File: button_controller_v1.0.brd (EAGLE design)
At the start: 160 x 100 mm, 88 parts, among them IC2 4051D, IC3 4520D, IC5 4051D

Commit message: Finished tracing
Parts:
- moved R6 18.4 mm to (74.3, 11.1)
- moved R1 14.3 mm to (78.7, 18.1), turned to 0 degrees
- moved R2 14.3 mm to (74.3, 18.1)
- moved R3 14.3 mm to (69.8, 18.1), turned to 0 degrees
- moved D14 11.1 mm to (11.4, 29.8)
- moved D17 11.1 mm to (37.5, 37.8)
- moved D22 11.1 mm to (37.5, 29.8)
- moved D25 11.1 mm to (24.4, 37.8)
- moved D30 11.1 mm to (24.4, 29.8)
- moved D33 11.1 mm to (63.5, 37.8)
- moved D38 11.1 mm to (63.5, 29.8)
- moved D41 11.1 mm to (50.5, 37.8)
- moved D46 11.1 mm to (50.5, 29.8)
- moved D57 11.1 mm to (76.5, 37.8)
- moved D62 11.1 mm to (76.5, 29.8)
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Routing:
- net +5V: track 75.1 -> 243.3 mm, vias 3 -> 7
- net RESET: track 0.00 -> 119.3 mm, vias 0 -> 4
- net CLK: track 0.00 -> 105.5 mm
- net BUTTON_VAL_CHAIN_2: track 0.00 -> 101.8 mm
- net BUTTON_VAL_CHAIN_4: track 0.00 -> 100.8 mm
- net BUTTON_VAL_CHAIN_1: track 0.00 -> 96.2 mm
- net BUTTON_VAL_CHAIN_3: track 0.00 -> 95.2 mm
- net BUTTON_VAL_CHAIN_5: track 0.00 -> 94.1 mm
- net BUTTON_VALUE: track 32.7 -> 105.8 mm, vias 2 -> 4
- net ROW7: track 33.5 -> 70.1 mm
- net ROW6: track 36.2 -> 67.6 mm, vias 0 -> 2
- net COL3: track 202.0 -> 178.3 mm
- net ROW5: track 32.1 -> 49.9 mm, vias 0 -> 2
- net COL2: track 189.1 -> 176.0 mm
- net COL4: track 212.9 -> 200.3 mm, vias 10 -> 8
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- added copper zone on layer 16, net GND
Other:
- board size 160 x 100 mm -> 105.7 x 44.1 mm

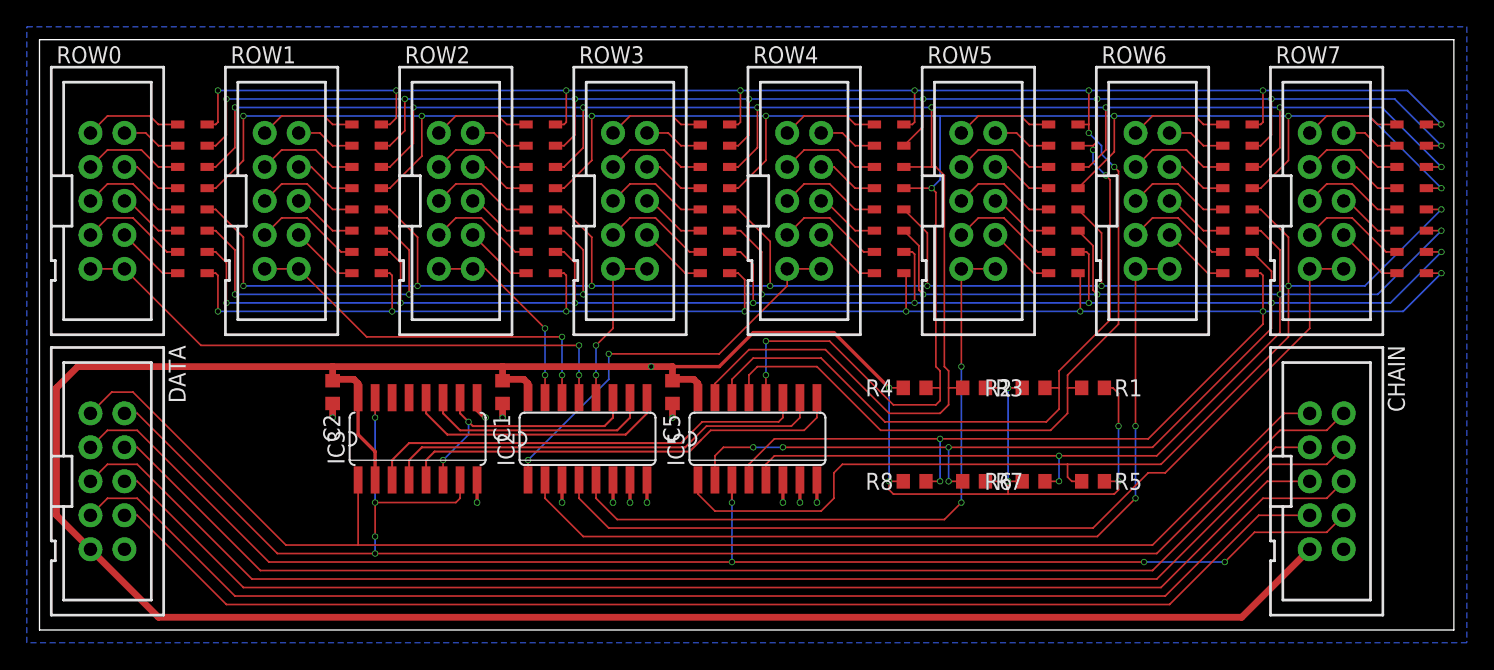
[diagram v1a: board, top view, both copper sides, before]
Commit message: Massive rerouting for a clearer separation between x and y direction
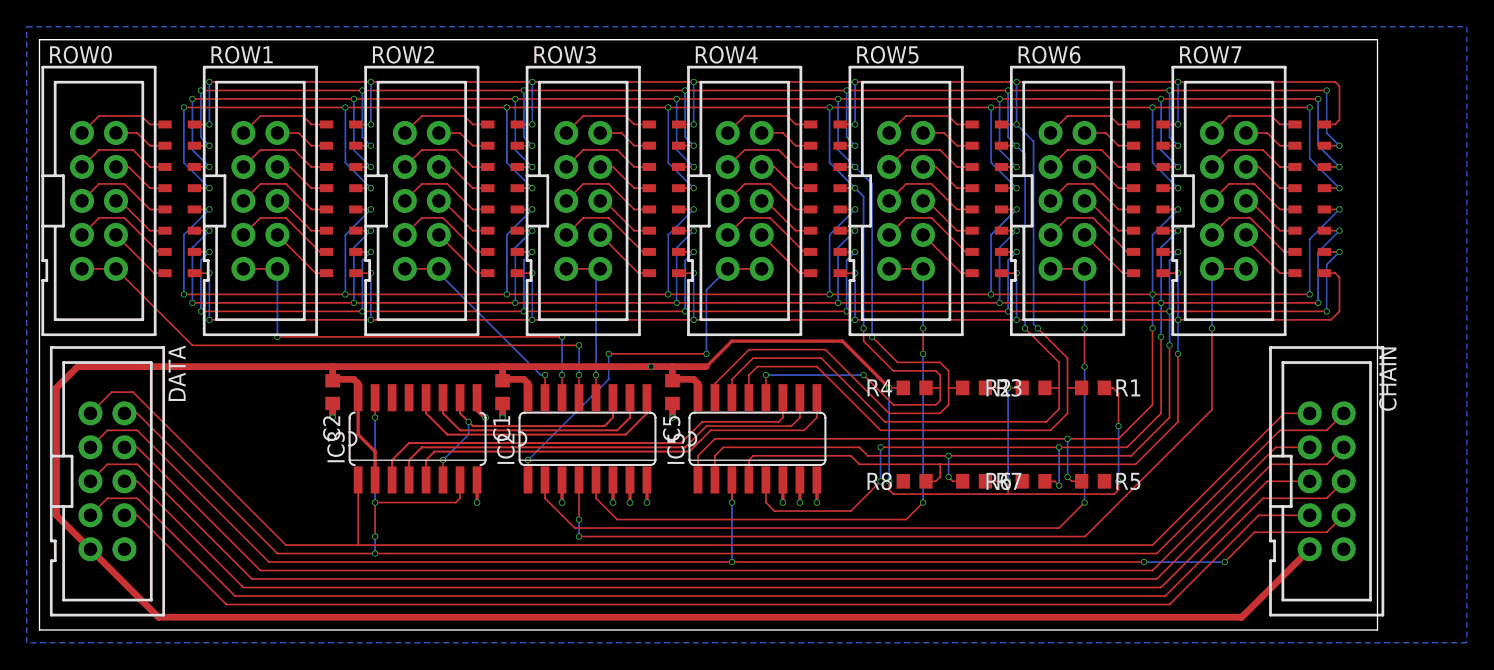
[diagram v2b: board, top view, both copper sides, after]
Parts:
- moved D89 7.62 mm to (94.9, 37.8)
- moved D90 7.62 mm to (94.9, 36.2)
- moved D91 7.62 mm to (94.9, 34.6)
- moved D92 7.62 mm to (94.9, 33.0)
- moved D93 7.62 mm to (94.9, 31.4)
- moved D94 7.62 mm to (94.9, 29.8)
- moved D95 7.62 mm to (94.9, 28.3)
- moved D96 7.62 mm to (94.9, 26.7)
- moved ROW7 7.30 mm to (88.9, 32.1)
- moved D73 6.67 mm to (82.9, 37.8)
- moved D74 6.67 mm to (82.9, 36.2)
- moved D75 6.67 mm to (82.9, 34.6)
- moved D76 6.67 mm to (82.9, 33.0)
- moved D77 6.67 mm to (82.9, 31.4)
- moved D78 6.67 mm to (82.9, 29.8)
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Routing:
- net COL2: track 176.0 -> 184.0 mm, vias 8 -> 17
- net COL3: track 178.3 -> 185.2 mm, vias 10 -> 19
- net COL5: track 183.7 -> 189.1 mm, vias 10 -> 21
- net ROW1: track 28.9 -> 33.8 mm, vias 2 -> 3
- net ROW6: track 67.6 -> 63.4 mm, vias 2 -> 3
- net +5V: track 243.3 -> 239.6 mm
- net COL1: track 176.3 -> 179.3 mm, vias 10 -> 17
- net ROW5: track 49.9 -> 47.0 mm, vias 2 -> 3
- net COL0: track 170.0 -> 172.4 mm, vias 10 -> 15
- net ROW4: track 31.2 -> 28.8 mm, vias 2 -> 3
- net ROW7: track 70.1 -> 68.5 mm, vias 0 -> 3
- net COL6: track 179.1 -> 179.8 mm, vias 12 -> 19
- net ROW2: track 15.0 -> 15.6 mm, vias 2 -> 1
- net ROW0: track 42.8 -> 43.4 mm
- net COL7: track 166.7 -> 167.3 mm, vias 10 -> 15
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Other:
- board size 105.7 x 44.1 mm -> 100 x 44.1 mm

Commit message: As small as it gets
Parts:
- moved R5 5.02 mm to (74.0, 9.53), turned to 270 degrees
- moved R1 4.77 mm to (74.0, 17.8), turned to 90 degrees
- moved R6 3.27 mm to (71.4, 9.53), turned to 270 degrees
- moved R2 2.88 mm to (71.4, 17.8), turned to 90 degrees
- moved R8 2.03 mm to (66.7, 9.53), turned to 270 degrees
- moved R7 1.71 mm to (69.2, 9.53), turned to 270 degrees
- moved D12 1.59 mm to (10.5, 31.4)
- moved D13 1.59 mm to (10.5, 29.8)
- moved D16 1.59 mm to (10.5, 25.1)
- moved D20 1.59 mm to (34.6, 31.4)
- moved D21 1.59 mm to (34.6, 29.8)
- moved D24 1.59 mm to (34.6, 25.1)
- moved D28 1.59 mm to (22.5, 31.4)
- moved D29 1.59 mm to (22.5, 29.8)
- moved D32 1.59 mm to (22.5, 25.1)
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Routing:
- net +5V: track 239.6 -> 231.9 mm, vias 7 -> 6
- net COL5: track 189.1 -> 182.3 mm
- net COL3: track 185.2 -> 178.8 mm
- net COL1: track 179.3 -> 173.9 mm
- net COL6: track 179.8 -> 175.6 mm
- net COL7: track 167.3 -> 163.2 mm
- net COL4: track 200.0 -> 196.3 mm
- net CLK: track 105.5 -> 109.1 mm
- net ROW7: track 68.5 -> 64.9 mm
- net BUTTON_VAL_CHAIN_1: track 96.2 -> 99.8 mm
- net BUTTON_VAL_CHAIN_2: track 101.8 -> 105.2 mm
- net BUTTON_VAL_CHAIN_3: track 95.2 -> 98.4 mm
- net RESET: track 119.3 -> 122.4 mm
- net COL0: track 172.4 -> 169.4 mm
- net BUTTON_VAL_CHAIN_4: track 100.8 -> 103.8 mm
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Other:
- board size 100 x 44.1 mm -> 100 x 40.6 mm

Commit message: Finished everything
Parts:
- added U$1: (no value), joakim:XONIK_LOGO_60
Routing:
- net ROW5: track 45.7 -> 43.4 mm, vias 1 -> 3
- net ROW6: track 62.1 -> 60.3 mm
- net COL3: track 178.8 -> 177.3 mm, vias 19 -> 18
- net +5V: track 231.9 -> 233.1 mm
- net COL_A: track 34.2 -> 33.3 mm
- net COL0: track 169.4 -> 170.3 mm
- net ROW2: track 15.9 -> 15.2 mm
- net COL1: track 173.9 -> 174.4 mm
- net COL7: track 163.2 -> 163.5 mm, vias 15 -> 14
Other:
- board text added: "+V"
- board text added: "4VOB"
- board text added: "8 x 8 key matrix scanner v1.0"
- board text added: "C1"
- board text added: "C2"
- board text added: "C3"
- board text added: "C4"
- board text added: "C5"
- board text added: "CLK"
- board text added: "GND"
- board text added: "Pin 1-8 = COL0-7 Pin 9,10 = ROW"
- board text added: "RST"
- board text added: "VAL"

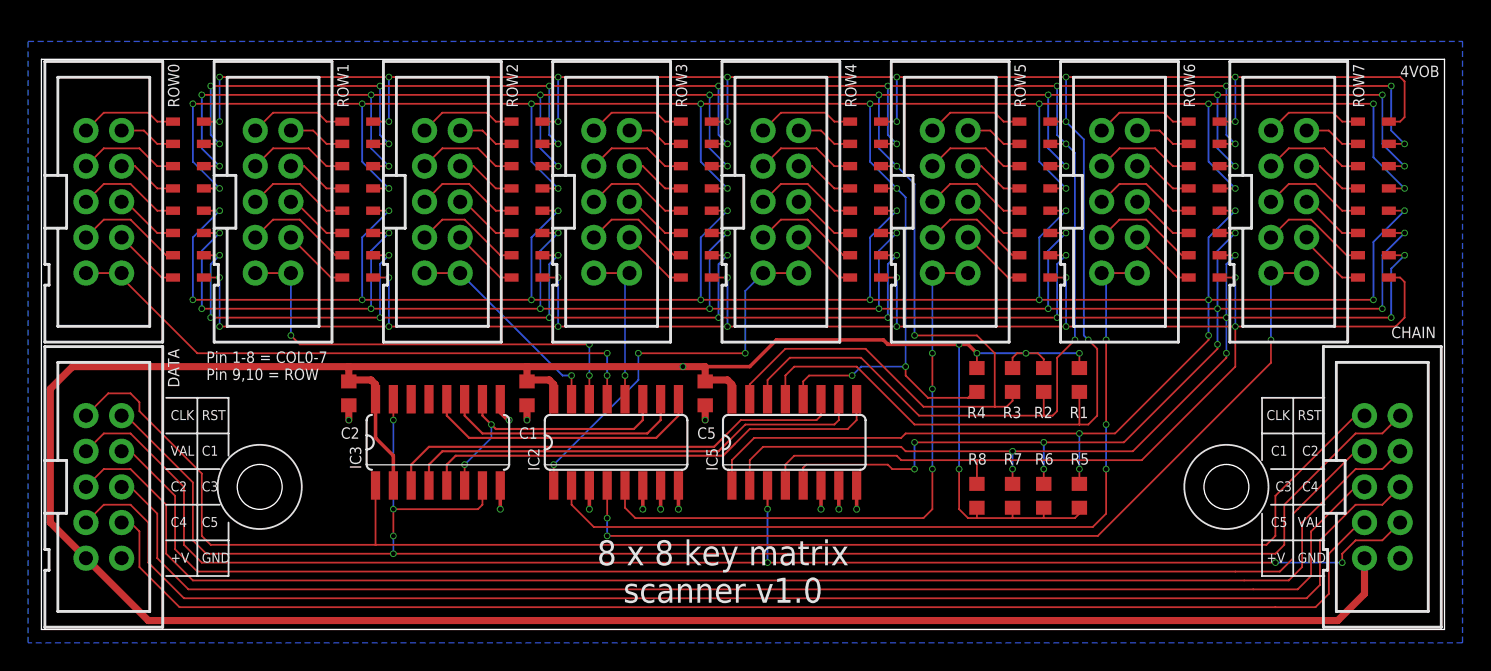
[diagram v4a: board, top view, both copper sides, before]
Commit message: Updated IDC connector size
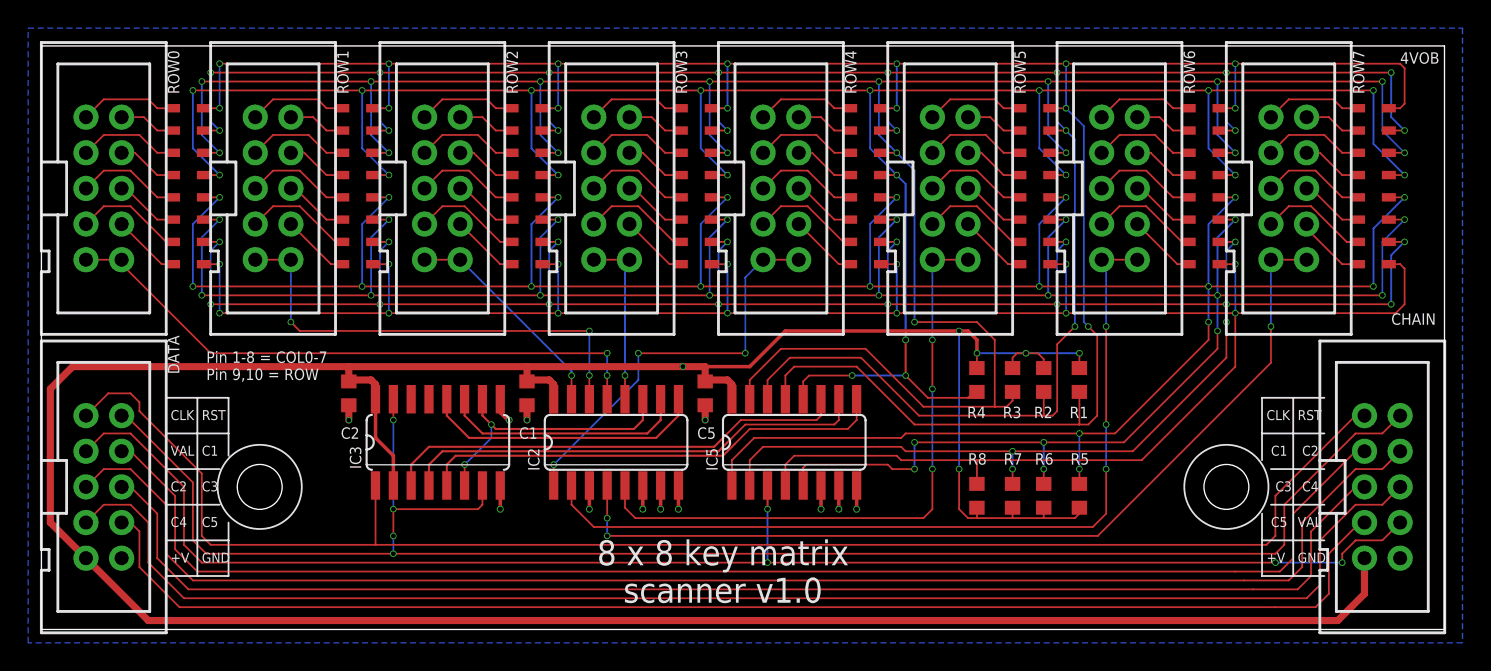
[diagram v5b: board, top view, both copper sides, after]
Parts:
- moved D10 0.95 mm to (10.5, 35.6)
- moved D13 0.95 mm to (10.5, 30.8)
- moved D14 0.95 mm to (10.5, 29.2)
- moved D16 0.95 mm to (10.5, 26.0)
- moved D17 0.95 mm to (34.6, 37.1)
- moved D18 0.95 mm to (34.6, 35.6)
- moved D21 0.95 mm to (34.6, 30.8)
- moved D22 0.95 mm to (34.6, 29.2)
- moved D24 0.95 mm to (34.6, 26.0)
- moved D25 0.95 mm to (22.5, 37.1)
- moved D26 0.95 mm to (22.5, 35.6)
- moved D29 0.95 mm to (22.5, 30.8)
- moved D30 0.95 mm to (22.5, 29.2)
- moved D32 0.95 mm to (22.5, 26.0)
- moved D33 0.95 mm to (58.7, 37.1)
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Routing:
- net +5V: track 233.1 -> 235.1 mm
- net COL2: track 184.6 -> 185.8 mm
- net COL7: track 163.5 -> 164.5 mm
- net COL5: track 182.3 -> 183.3 mm
- net COL0: track 170.3 -> 171.2 mm
- net ROW7: track 64.9 -> 65.9 mm
- net ROW6: track 60.3 -> 61.3 mm
- net ROW5: track 43.4 -> 44.4 mm
- net ROW4: track 28.3 -> 29.3 mm
- net ROW3: track 11.7 -> 12.6 mm
- net ROW1: track 32.4 -> 33.4 mm
- net COL6: track 175.9 -> 176.8 mm
- net COL1: track 174.4 -> 175.4 mm
- net COL4: track 196.3 -> 197.2 mm
- net COL3: track 177.3 -> 178.0 mm, vias 18 -> 19
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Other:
- board size 100 x 40.6 mm -> 100 x 41.6 mm
